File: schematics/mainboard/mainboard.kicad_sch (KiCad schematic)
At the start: 36 parts, among them J1 SD_Card_Receptacle, J2 Conn_02x20_Odd_Even_MountingP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, J3 USB_C_Receptacle_USB2.0_16P, J4 Conn_01x03, P1 1-1473005-4, U1 TLV75801PDBV, U2 TLV75801PDBV, U3 MAX3421EETJ_T, U5 BQ24040DSQR, U6 TPS63002, U7 TLV75801PDBV

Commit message: More mainboard schematics work.
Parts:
- added C16: 1u, Capacitor_SMD:C_0805_2012Metric, symbol Device:C
- added C17: 10u, Capacitor_SMD:C_0805_2012Metric, symbol Device:C
- added C18: 0.1u, Capacitor_SMD:C_0805_2012Metric, symbol Device:C
- added L1: L, Inductor_SMD:L_1008_2520Metric, symbol Device:L
- added R5: 100, Resistor_SMD:R_0805_2012Metric_Pad1.20x1.40mm_HandSolder, symbol Device:R
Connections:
- net 5V0: now also C16.2
- net BAT+: now also C17.2, R5.2
- net GND: now also C16.1, C17.1, C18.1
- net LCD_PROG_DATA: now also P1.104
- net LCD_TOUCH_CLK: now also P1.102
- net LCD_TOUCH_DATA: now also P1.100
- net LCD_TOUCH_INTERRUPT: now also P1.98
- net at U6.2 (L2): now also L1.1
- net at U6.4 (L1): now also L1.2
- net at U6.6 (EN): now also U6.7 (PS/SYNC), U6.8 (VINA), C18.2, R5.1
- no-connect marks 70 -> 71
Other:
- note added: "Switch current min 1600 mA"
- moved on the sheet: TP_5V0

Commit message: Trace length tuned for LCD and SRAM. Also reduced size of board a bit.
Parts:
- removed U1, U2, U7: TLV75801PDBV, Package_TO_SOT_SMD:SOT-23-5, symbol Regulator_Linear:TLV75801PDBV
- added C19, C20: C, Capacitor_SMD:C_0805_2012Metric, symbol Device:C
- added C21, C22, C23, C24: 10nF, Capacitor_SMD:C_0805_2012Metric_Pad1.18x1.45mm_HandSolder, symbol pspice:C
- added C25, C26: 100uF, Capacitor_SMD:CP_Elec_5x5.3, symbol Device:C_Polarized
- added J6: Conn_01x12, Connector_PinHeader_2.54mm:PinHeader_1x12_P2.54mm_Vertical, symbol Connector_Generic:Conn_01x12
- added R10, R11, R12, R13, R14, R15, R16, R8, R9: 10k, Resistor_SMD:R_0805_2012Metric_Pad1.20x1.40mm_HandSolder, symbol Device:R
- added R17, R18, R19, R20: 4k7, Resistor_SMD:R_0805_2012Metric_Pad1.20x1.40mm_HandSolder, symbol Device:R
- added R6, R7: 5.1k, Resistor_SMD:R_0805_2012Metric_Pad1.20x1.40mm_HandSolder, symbol Device:R
- added SW1: SW_SPST, symbol Switch:SW_SPST
- added U1, U2, U9: AMS1117-3.3, Package_TO_SOT_SMD:SOT-223-3_TabPin2, symbol Regulator_Linear:AMS1117-3.3
- added U8: MAX9715xTE+, Package_DFN_QFN:TQFN-16-1EP_5x5mm_P0.8mm_EP3.1x3.1mm, symbol Amplifier_Audio:MAX9715xTE+
- added Y1: Crystal, Crystal:Crystal_SMD_2012-2Pin_2.0x1.2mm_HandSoldering, symbol Device:Crystal
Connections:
- net 3V3: now also R10.2, R11.2, R12.2, R13.2, R14.2, R15.2, R16.2, R8.2, R9.2, U2.2 (VO)
- net 3V3_LCD: now also U1.2 (VO)
- net 3V3_SD: now also U9.2 (VO)
- net 5V0: now also U1.3 (VI), U2.3 (VI), U9.3 (VI)
- net BAT+: now also SW1.1 (A); no longer C17.2, R5.2, U6.5 (VIN)
- net GND: now also C19.1, C20.1, J6.1 (Pin_1), R6.1, R7.1, U1.1 (GND), U2.1 (GND), U8.1 (PGND), U8.12 (PGND), U8.17 (PAD), U8.7 (GND), U9.1 (GND)
- net SRAM_A0: now also P1.113; no longer P1.89
- net SRAM_A1: now also P1.117; no longer P1.91
- net SRAM_A10: now also P1.103; no longer P1.131
- net SRAM_A11: now also P1.99; no longer P1.133
- net SRAM_A12: now also P1.95; no longer P1.135
- net SRAM_A13: now also P1.91; no longer P1.137
- net SRAM_A14: now also P1.87; no longer P1.139
- net SRAM_A15: now also P1.85; no longer P1.77
- net SRAM_A16: now also P1.89; no longer P1.79
- net SRAM_A17: now also P1.93; no longer P1.81
- net SRAM_A18: now also P1.97; no longer P1.83
- net SRAM_A19: now also P1.101; no longer P1.85
- net SRAM_A2: now also P1.121; no longer P1.93
- net SRAM_A3: now also P1.125; no longer P1.95
- net SRAM_A4: now also P1.129; no longer P1.97
- net SRAM_A5: now also P1.131; no longer P1.119
- net SRAM_A6: now also P1.127; no longer P1.121
- net SRAM_A8: now also P1.119; no longer P1.125
- net SRAM_A9: now also P1.115; no longer P1.127
- net SRAM_D0: now also P1.81; no longer P1.75
- net SRAM_D1: now also P1.77; no longer P1.73
- net SRAM_D10: now also P1.143; no longer P1.113
- net SRAM_D11: now also P1.147; no longer P1.111
- net SRAM_D12: now also P1.145; no longer P1.109
- net SRAM_D13: now also P1.141; no longer P1.103
- net SRAM_D14: now also P1.137; no longer P1.101
- net SRAM_D15: now also P1.133; no longer P1.99
- net SRAM_D2: now also P1.73; no longer P1.71
- net SRAM_D4: now also P1.71; no longer P1.147
- net SRAM_D5: now also P1.75; no longer P1.145
- net SRAM_D6: now also P1.79; no longer P1.143
- net SRAM_D7: now also P1.83; no longer P1.141
- net SRAM_D8: now also P1.135; no longer P1.117
- net SRAM_D9: now also P1.139; no longer P1.115
- net ~{SRAM_OE}: now also P1.111; no longer P1.129
- net ~{SRAM_WE}: now also P1.109; no longer P1.87
- net at J3.A5 (CC1): now also R7.2
- net at J3.B5 (CC2): now also R6.2
- net USB_HCI_XI: now reaches U3.24 (XI)
- net USB_HCI_XI: now also C19.2, Y1.1
- net USB_HCI_XO: now reaches U3.25 (XO)
- net USB_HCI_XO: now also C20.2, Y1.2
- net HIO_BTN_X: now reaches P1.80
- net HIO_BTN_X: now also J6.10 (Pin_10), R16.1
- net HIO_BTN_D: now reaches P1.82
- net HIO_BTN_D: now also J6.9 (Pin_9), R15.1
- net HIO_BTN_C: now reaches P1.84
- net HIO_BTN_C: now also J6.8 (Pin_8), R11.1
- net HIO_BTN_B: now reaches P1.86
- net HIO_BTN_B: now also J6.7 (Pin_7), R14.1
- net HIO_BTN_A: now reaches P1.88
- net HIO_BTN_A: now also J6.6 (Pin_6), R10.1
- net HIO_DPAD_E: now reaches P1.90
- net HIO_DPAD_E: now also J6.5 (Pin_5), R13.1
- net HIO_DPAD_W: now reaches P1.92
- net HIO_DPAD_W: now also J6.4 (Pin_4), R9.1
- net HIO_DPAD_S: now reaches P1.94
- net HIO_DPAD_S: now also J6.3 (Pin_3), R12.1
- net HIO_DPAD_N: now reaches P1.96
- net HIO_DPAD_N: now also J6.2 (Pin_2), R8.1
- new net: C21.1, R17.2, R19.1
- new net: C24.2, C26.1, R20.2
- new net: C26.2, U8.15 (INR)
- new net: C21.2, C22.1, C23.2, C24.1
- new net: C23.1, C25.1, R19.2
- new net: C25.2, U8.16 (INL)
- new net: U8.4 (PVDD), U8.9 (PVDD)
- new net: C22.2, R18.2, R20.1
- new net PWM_L: R17.1
- new net PWM_R: R18.1
- new net SYS_LOAD: C17.2, R5.2, SW1.2 (B), U6.5 (VIN)
- no-connect marks 71 -> 73
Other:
- moved on the sheet: J3

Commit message: More work on mainboard schematic.
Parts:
- removed C8: 1u, Capacitor_SMD:C_0805_2012Metric, symbol Device:C
- added C27: 10uF, Capacitor_SMD:CP_Elec_5x5.3, symbol Device:C_Polarized
- added R21, R22, R23, R24, R25: 4k7, Resistor_SMD:R_0805_2012Metric_Pad1.20x1.40mm_HandSolder, symbol Device:R
- C19, C20: value C -> 27pF
- J2: symbol Connector_Generic_MountingPin:Conn_02x20_Odd_Even_MountingPin -> Connector_Generic:Conn_02x20_Odd_Even
- Y1: value Crystal -> 12MHz; footprint Crystal:Crystal_SMD_2012-2Pin_2.0x1.2mm_HandSoldering -> Crystal:Crystal_SMD_HC49-SD
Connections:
- net 3V3_SD: now also R21.2, R22.2, R23.2, R24.2, R25.2
- net 5V0: now also U8.14 (VDD), U8.4 (PVDD), U8.9 (PVDD)
- net GND: now also C27.2
- net SD_CMD: now also R25.1
- net SD_DAT0: now also R21.1
- net SD_DAT1: now also R22.1
- net SD_DAT2: now also R23.1
- net SD_DAT3: now also R24.1
- net USB_VBUS: now also C27.1
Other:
- moved on the sheet: J1

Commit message: Mainboard schematics, audio system and power traces.
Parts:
- removed C1, C2: C, Capacitor_SMD:C_0805_2012Metric, symbol Device:C
- removed C17: 10u, Capacitor_SMD:C_0805_2012Metric, symbol Device:C
- removed TP1: TP_3V3_SD, TestPoint:TestPoint_Pad_D1.5mm, symbol Connector:TestPoint
- removed TP2: TP_3V3_LCD, TestPoint:TestPoint_Pad_D1.5mm, symbol Connector:TestPoint
- removed TP3: TP_3V3, TestPoint:TestPoint_Pad_D1.5mm, symbol Connector:TestPoint
- removed TP_5V0: TP_5V0, TestPoint:TestPoint_Pad_D1.5mm, symbol Connector:TestPoint
- removed TP_VBUS1: TP_VBUS, TestPoint:TestPoint_Pad_D1.5mm, symbol Connector:TestPoint
- removed U5: BQ24040DSQR, BQ24040DSQR:SON40P200X200X80-11N, symbol BQ24040DSQR:BQ24040DSQR
- removed U9: AMS1117-3.3, Package_TO_SOT_SMD:SOT-223-3_TabPin2, symbol Regulator_Linear:AMS1117-3.3
- added C1, C17, C30: 10uF, Capacitor_SMD:CP_Elec_5x5.3, symbol Device:C_Polarized
- added C2, C31: 22uF, Capacitor_SMD:CP_Elec_5x5.3, symbol Device:C_Polarized
- added C28, C29: 10uF, Capacitor_SMD:C_0805_2012Metric, symbol Device:C
- added C8: 1uF, Capacitor_SMD:C_0805_2012Metric, symbol Device:C
- added D1, D3: LED, LED_SMD:LED_0805_2012Metric, symbol Device:LED
- added H1, H2, H3, H4: MountingHole, MountingHole:MountingHole_2.5mm, symbol Mechanical:MountingHole
- added J5: Conn_01x03_Pin, Connector_PinHeader_2.54mm:PinHeader_1x03_P2.54mm_Vertical, symbol Connector:Conn_01x03_Pin
- added J7: AudioJack3_Switch, symbol Connector_Audio:AudioJack3_Switch
- added LS1, LS2: Speaker, symbol Device:Speaker
- added R26, R27: 1k, Resistor_SMD:R_0805_2012Metric_Pad1.20x1.40mm_HandSolder, symbol Device:R
- added R28: 10k, Resistor_SMD:R_0805_2012Metric_Pad1.20x1.40mm_HandSolder, symbol Device:R
- added U7: BQ24072RGT, Package_DFN_QFN:VQFN-16-1EP_3x3mm_P0.5mm_EP1.6x1.6mm, symbol Battery_Management:BQ24072RGT
- C10, C11, C12, C13, C14, C15, C3, C4, C5, C6: value C -> 1uF
- C16: value 1u -> 10uF
- C25, C26: value 100uF -> 47uF; footprint Capacitor_SMD:CP_Elec_5x5.3 -> Capacitor_Tantalum_SMD:CP_EIA-3216-18_Kemet-A
- C7: value 1u -> 1uF
- C9: value 1u -> 4.7uF
- J4: value Conn_01x03 -> Conn_01x02; footprint (none) -> Connector_JST:JST_PH_S2B-PH-K_1x02_P2.00mm_Horizontal; symbol Connector_Generic:Conn_01x03 -> Connector_Generic:Conn_01x02
- L1: value L -> 2.2uH; footprint Inductor_SMD:L_1008_2520Metric -> Inductor_SMD:L_APV_ANR4012
- R3: value 540 -> 1.18k
- R4: value 2k -> 1.13k
- SW1: footprint (none) -> Connector_PinHeader_1.00mm:PinHeader_1x02_P1.00mm_Vertical
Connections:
- net 3V3_SD is gone; now on net 3V3_LCD: C4.2, J1.4 (VDD), R21.2, R22.2, R23.2, R24.2, R25.2
- net 3V3: now also C31.1, C8.2; no longer C15.2
- net 3V3_LCD: now also C3.2, C2.1
- net 5V0: now also U6.10 (FB), U8.8 (~{SHDN}), C1.1, C29.2, C30.1, J5.1 (Pin_1); no longer C3.2
- net BAT+: now also U7.2 (BAT), U7.3 (BAT); no longer SW1.1 (A)
- net GND: now also C15.2, C21.2, C22.1, C23.2, C24.1, J4.2 (Pin_2), R3.2, R4.2, C1.2, C17.2, C2.2, C28.1, C29.1, C30.2, C31.2, C8.1, J5.3 (Pin_3), R28.2, U7.17 (VSS), U7.4 (~{CE}), U7.6 (EN1), U7.8 (VSS); no longer C15.1, J4.3 (Pin_3), R3.1, R4.1
- net SYS_LOAD: now also C17.1
- net USB_VBUS: now also U7.13 (IN)
- net at U8.10 (OUTR-): now also LS2.2
- net at U8.11 (OUTR+): now also LS2.1
- net at U8.13 (BIAS): now also C15.1
- net at U8.2 (OUTL+): now also LS1.1
- net at U8.3 (OUTL-): now also LS1.2
- net at U8.6 (GAIN): now also J5.2 (Pin_2)
- new net: C28.2, R26.1, R27.1, SW1.1 (A), U7.10 (OUT), U7.11 (OUT), U7.15 (TD), U7.5 (EN2)
- new net: D3.2 (A), R26.2
- new net: D3.1 (K), U7.7 (~{PGOOD})
- new net: D1.1 (K), U7.9 (~{CHG})
- new net: D1.2 (A), R27.2
- new net: R28.1, U7.1 (TS)
- new net: R4.1, U7.16 (ISET)
- new net: R3.1, U7.12 (ILIM)
- no-connect marks 73 -> 72
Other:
- note added: "Battery terminal JST-PH"
- note removed: "Battery terminal (+temp sensor)"
- moved on the sheet: C27, C9, R10, R11, R12, R13, R14, R15, R16, R8, R9, SW1

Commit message: SD card connector fixed in schematics. Added JLCPBC part numbers to some components.
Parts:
- added C32: 1uF, Capacitor_SMD:C_0805_2012Metric, symbol Device:C
- added R29: 57k, Resistor_SMD:R_0805_2012Metric_Pad1.20x1.40mm_HandSolder, symbol Device:R
- C25, C26: LCSC (none) -> C7190
- J1: footprint Connector_Card:SD_Hirose_DM1AA_SF_PEJ82 -> DM1AA-SF-PEJ(82):RetroDACK SD_Hirose_DM1AA_SF_PEJ82; LCSC (none) -> C506790
- L1: LCSC (none) -> C36409
- P1: LCSC (none) -> C428482
- U3: LCSC (none) -> C2651881
- U4: LCSC (none) -> C2959389
- U6: LCSC (none) -> C116655
- U7: LCSC (none) -> C81080
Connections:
- net 3V3_LCD: now also R29.2
- net 5V0: now also C32.2
- net GND: now also C32.1
- net SD_CARD: now reaches J1.10 (CARD_DETECT)
- net SD_CARD: now also R29.1
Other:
- moved on the sheet: C15, C19, C20, C21, C22, C23, C24, C25, C26, C3, C4, C5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

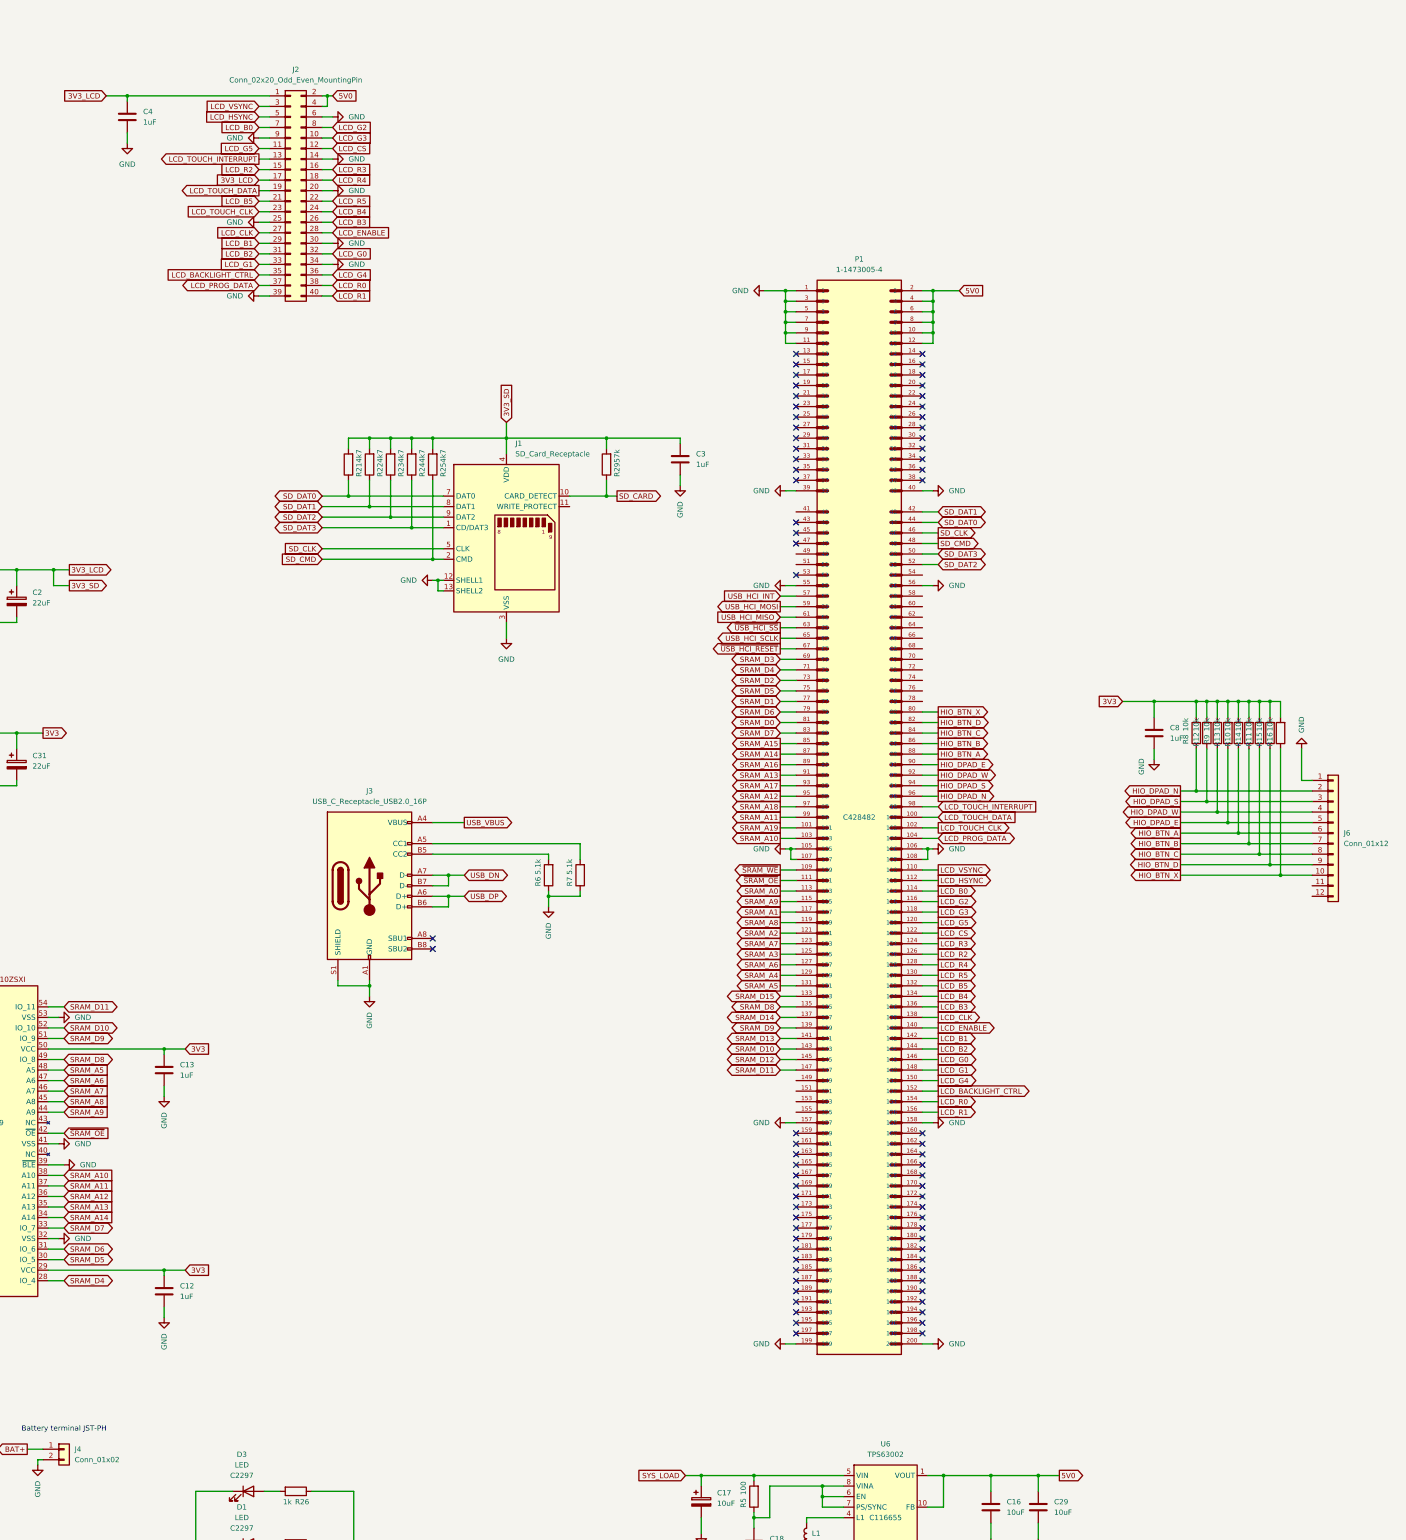
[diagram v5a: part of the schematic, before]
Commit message: Added connector for trackball to mainboard schematics.
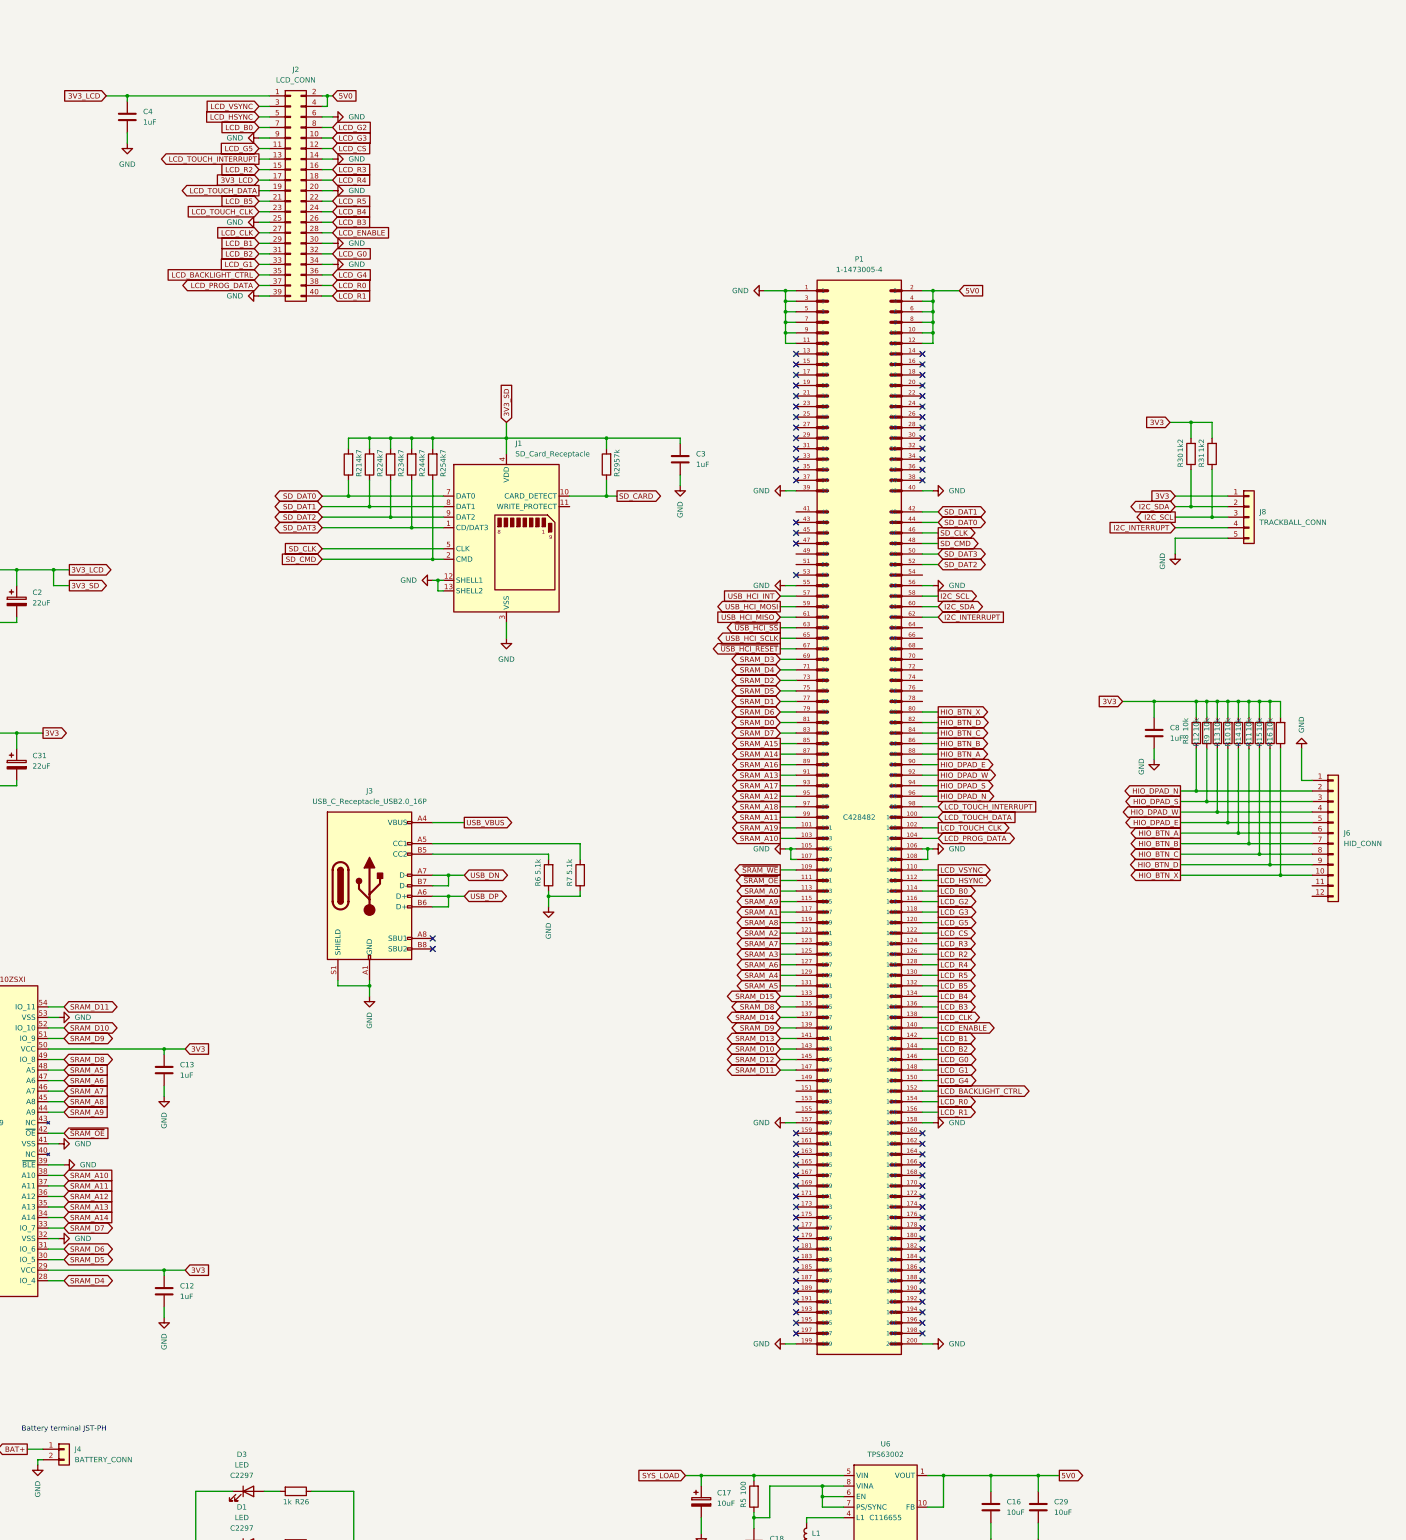
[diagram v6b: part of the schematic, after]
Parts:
- added J8: TRACKBALL_CONN, Connector_PinHeader_2.54mm:PinHeader_1x05_P2.54mm_Vertical, symbol Connector_Generic:Conn_01x05
- added R30, R31: 1k2, Resistor_SMD:R_0805_2012Metric_Pad1.20x1.40mm_HandSolder, symbol Device:R
- J2: value Conn_02x20_Odd_Even_MountingPin -> LCD_CONN
- J4: value Conn_01x02 -> BATTERY_CONN
- J6: value Conn_01x12 -> HID_CONN
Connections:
- net 3V3: now also J8.1 (Pin_1), R30.2, R31.2
- net GND: now also J8.5 (Pin_5)
- net I2C_SCL: now reaches P1.58
- net I2C_SCL: now also J8.3 (Pin_3), R31.1
- net I2C_SDA: now reaches P1.60
- net I2C_SDA: now also J8.2 (Pin_2), R30.1
- net I2C_INTERRUPT: now reaches P1.62
- net I2C_INTERRUPT: now also J8.4 (Pin_4)
